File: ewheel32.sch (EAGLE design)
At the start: 201 parts, among them Q1 32.768kHz, Q2 8MHz, U1 MK22DX256VLF5, U10 MC74HC595ADTR2G, U11 MC74HC595ADTR2G, U12 MC74HC595ADTR2G, U13 MC74HC595ADTR2G, U14 MC74HC595ADTR2G, U15 MC74HC595ADTR2G, U16 MC74HC595ADTR2G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

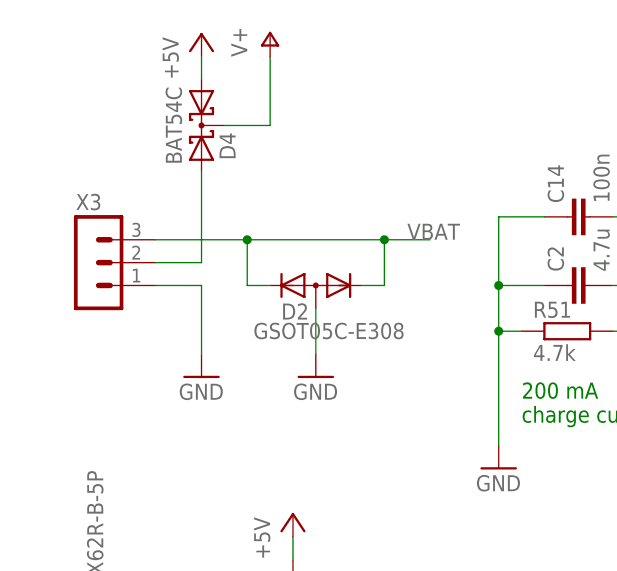
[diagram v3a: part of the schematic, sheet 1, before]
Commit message: VBAT and V+ are fixed.
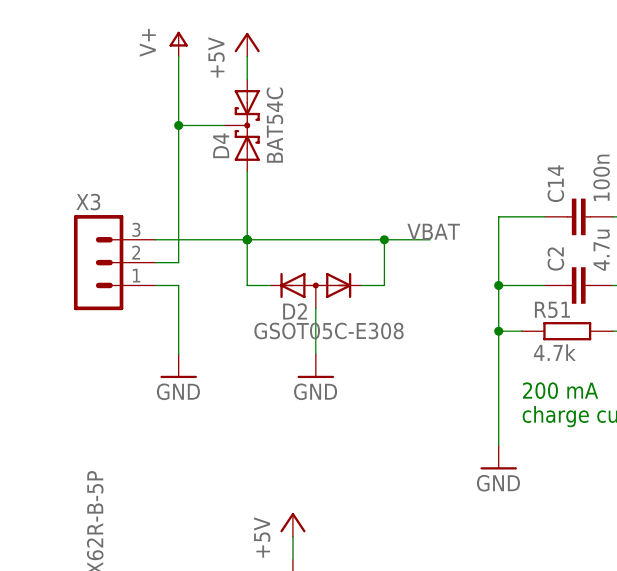
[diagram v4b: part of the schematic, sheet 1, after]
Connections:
- removed net N$6: D4.A2, X3.2
- net V+: now also X3.2
- net VBAT: now also D4.A2
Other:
- moved on the sheet: D4
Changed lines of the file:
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@@
 </instance>
 <instance part="X3" gate="G$1" x="17.78" y="226.06"/>
-<instance part="P+1" gate="1" x="38.1" y="251.46"/>
+<instance part="P+1" gate="1" x="27.94" y="251.46"/>
 <instance part="P+3" gate="1" x="203.2" y="233.68"/>
-<instance part="GND2" gate="1" x="30.48" y="213.36"/>
+<instance part="GND2" gate="1" x="27.94" y="213.36"/>
 <instance part="GND4" gate="1" x="93.98" y="203.2"/>
 <instance part="GND6" gate="1" x="144.78" y="35.56"/>
@@
 <instance part="GND49" gate="1" x="48.26" y="88.9"/>
 <instance part="D3" gate="G$1" x="43.18" y="111.76" rot="R270"/>
-<instance part="D4" gate="G$1" x="30.48" y="241.3" rot="R270"/>
+<instance part="D4" gate="G$1" x="35.56" y="241.3" rot="MR270"/>
 <instance part="C24" gate="G$1" x="55.88" y="142.24"/>
 <instance part="GND50" gate="1" x="55.88" y="132.08"/>
@@
 <instance part="R60" gate="G$1" x="116.84" y="241.3"/>
 <instance part="GND55" gate="1" x="124.46" y="236.22"/>
-<instance part="P+6" gate="1" x="30.48" y="251.46"/>
+<instance part="P+6" gate="1" x="35.56" y="251.46"/>
 </instances>
 <busses>
@@
 <segment>
 <pinref part="X3" gate="G$1" pin="1"/>
-<wire x1="25.4" y1="223.52" x2="30.48" y2="223.52" width="0.1524" layer="91"/>
-<wire x1="30.48" y1="223.52" x2="30.48" y2="215.9" width="0.1524" layer="91"/>
+<wire x1="25.4" y1="223.52" x2="27.94" y2="223.52" width="0.1524" layer="91"/>
+<wire x1="27.94" y1="223.52" x2="27.94" y2="215.9" width="0.1524" layer="91"/>
 <pinref part="GND2" gate="1" pin="GND"/>
 </segment>
@@
 <segment>
 <pinref part="P+1" gate="1" pin="V+"/>
-<wire x1="38.1" y1="248.92" x2="38.1" y2="241.3" width="0.1524" layer="91"/>
+<wire x1="27.94" y1="248.92" x2="27.94" y2="241.3" width="0.1524" layer="91"/>
 <pinref part="D4" gate="G$1" pin="CC"/>
-<wire x1="33.02" y1="241.3" x2="38.1" y2="241.3" width="0.1524" layer="91"/>
+<wire x1="33.02" y1="241.3" x2="27.94" y2="241.3" width="0.1524" layer="91"/>
+<pinref part="X3" gate="G$1" pin="2"/>
+<wire x1="25.4" y1="226.06" x2="27.94" y2="226.06" width="0.1524" layer="91"/>
+<wire x1="27.94" y1="226.06" x2="27.94" y2="241.3" width="0.1524" layer="91"/>
+<junction x="27.94" y="241.3"/>
 </segment>
 <segment>
@@
 <pinref part="D4" gate="G$1" pin="A1"/>
 <pinref part="P+6" gate="1" pin="+5V"/>
-<wire x1="30.48" y1="246.38" x2="30.48" y2="248.92" width="0.1524" layer="91"/>
+<wire x1="35.56" y1="246.38" x2="35.56" y2="248.92" width="0.1524" layer="91"/>
 </segment>
 </net>
@@
 <wire x1="38.1" y1="223.52" x2="35.56" y2="223.52" width="0.1524" layer="91"/>
 <wire x1="35.56" y1="223.52" x2="35.56" y2="228.6" width="0.1524" layer="91"/>
+<pinref part="D2" gate="G$1" pin="K1"/>
 <wire x1="35.56" y1="228.6" x2="25.4" y2="228.6" width="0.1524" layer="91"/>
-<pinref part="D2" gate="G$1" pin="K1"/>
 <wire x1="48.26" y1="223.52" x2="50.8" y2="223.52" width="0.1524" layer="91"/>
 <wire x1="50.8" y1="223.52" x2="50.8" y2="228.6" width="0.1524" layer="91"/>
@@
 <junction x="50.8" y="228.6"/>
 <label x="53.34" y="228.6" size="1.778" layer="95"/>
+<pinref part="D4" gate="G$1" pin="A2"/>
+<wire x1="35.56" y1="236.22" x2="35.56" y2="228.6" width="0.1524" layer="91"/>
+<junction x="35.56" y="228.6"/>
 </segment>
 <segment>
@@
 </segment>
 </net>
-<net name="N$6" class="0">
-<segment>
-<pinref part="D4" gate="G$1" pin="A2"/>
-<wire x1="30.48" y1="236.22" x2="30.48" y2="226.06" width="0.1524" layer="91"/>
-<pinref part="X3" gate="G$1" pin="2"/>
-<wire x1="30.48" y1="226.06" x2="25.4" y2="226.06" width="0.1524" layer="91"/>
-</segment>
-</net>

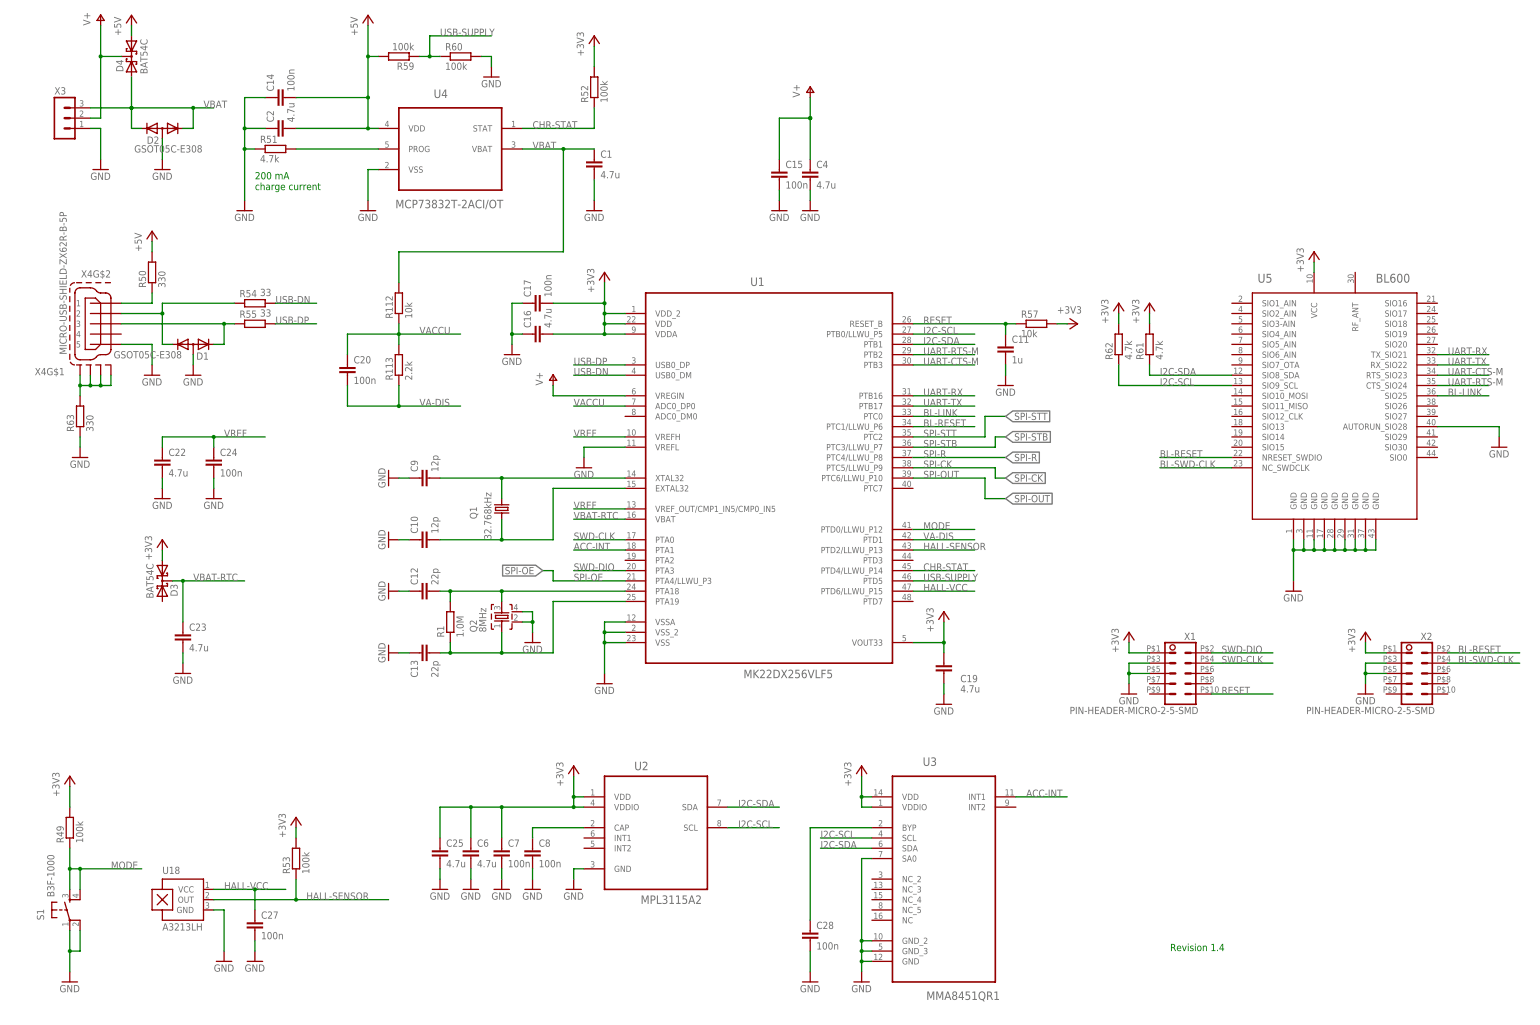
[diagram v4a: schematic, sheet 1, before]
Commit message: State RGB LED. Second Hall Sensor (ultra low power to wake up from deep sleep). Breakable PCB (MCU part / LED part). Pin head for I2C and SPI.
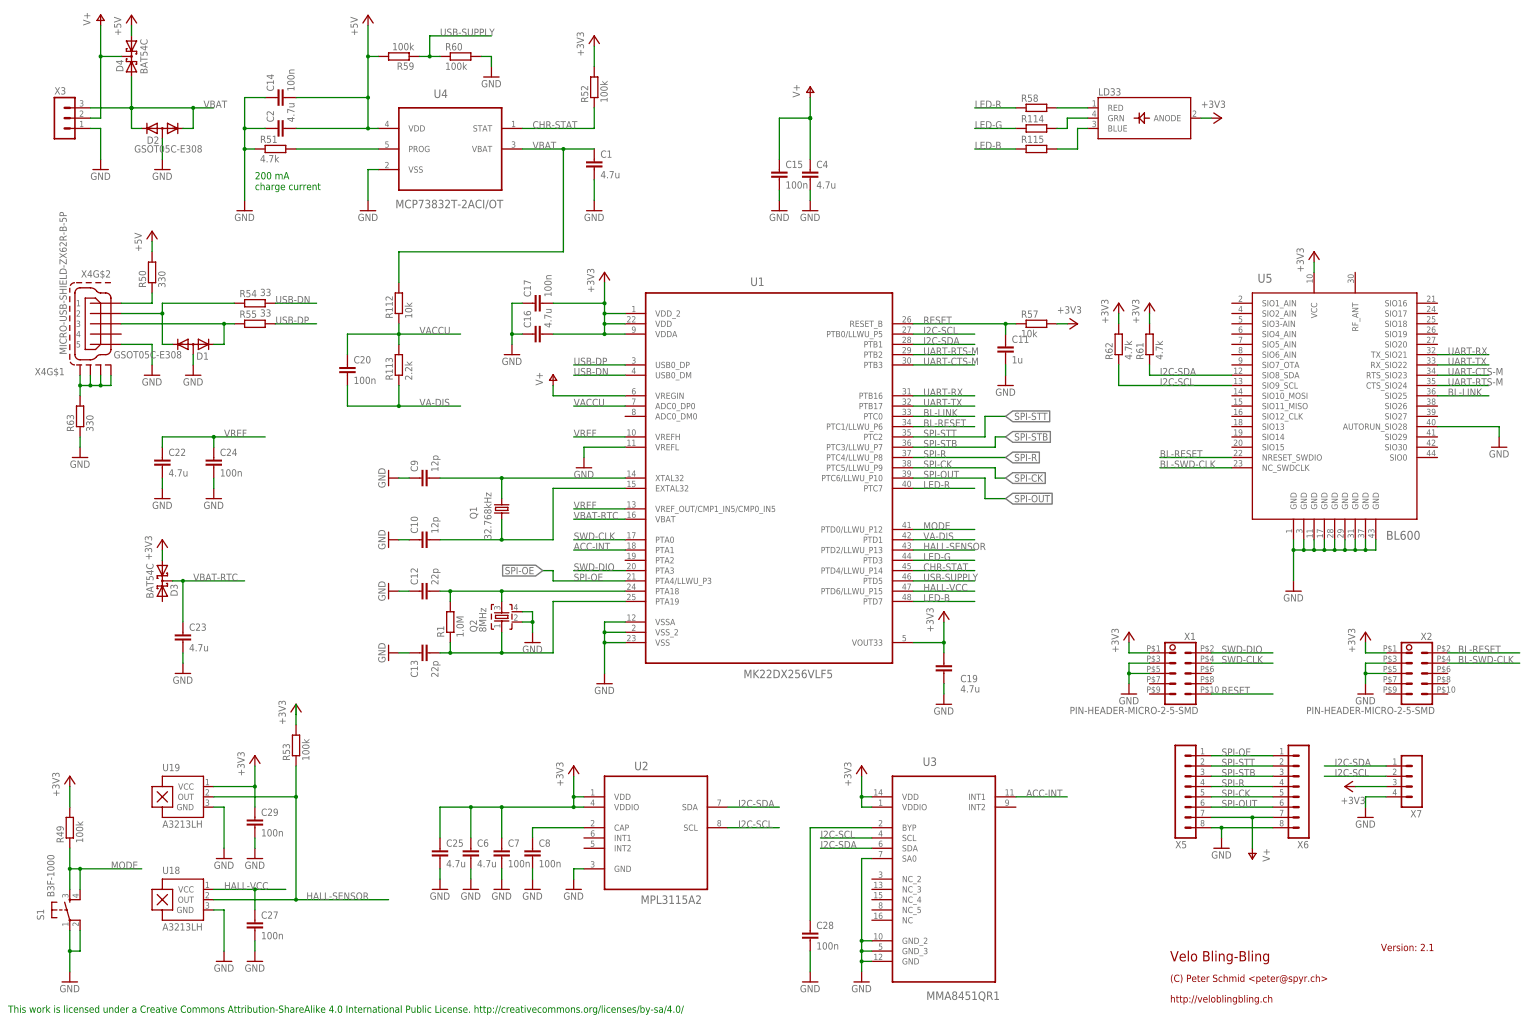
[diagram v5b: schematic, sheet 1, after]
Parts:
- added C29: 100n, resistor:C-EUC0805
- added LD33: CLV1A-FKB, freescale-uc:LED-RGB
- added R114, R115, R58: 220, resistor:R-EU_R0805
- added U19: A3213LH, allegro:A1381LH
- added X5, X6: (no value), con-lstb:MA08-1
- added X7: (no value), con-lstb:MA04-1
- C1, C11, C16, C18, C19, C2, C21, C22, C23, C25, C4, C6: device resistor:C-EUC1206 -> resistor:C-EUC0805
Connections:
- new net LED-B: R115.1, U1.PTD7
- new net LED-G: R114.1, U1.PTD3
- new net LED-R: R58.1, U1.PTC7
- new net N$6: LD33.GRN, R114.2
- new net N$7: LD33.RED, R58.2
- new net N$8: LD33.BLUE, R115.2
- net +3V3: now also C29.1, LD33.ANODE, U19.VCC, X7.3
- net GND: now also C29.2, U19.GND, X5.8, X6.8, X7.4
- net HALL-SENSOR: now also U19.OUT
- net I2C-SCL: now also X7.2
- net I2C-SDA: now also X7.1
- net SPI-CK: now also X5.5, X6.5
- net SPI-OE: now also X5.1, X6.1
- net SPI-OUT: now also X5.6, X6.6
- net SPI-R: now also X5.4, X6.4
- net SPI-STB: now also X5.3, X6.3
- net SPI-STT: now also X5.2, X6.2
- net V+: now also X5.7, X6.7
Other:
- note removed: "Revision 1.4"
- moved on the sheet: R53

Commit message: New Bluetooth Low Energy module BL652
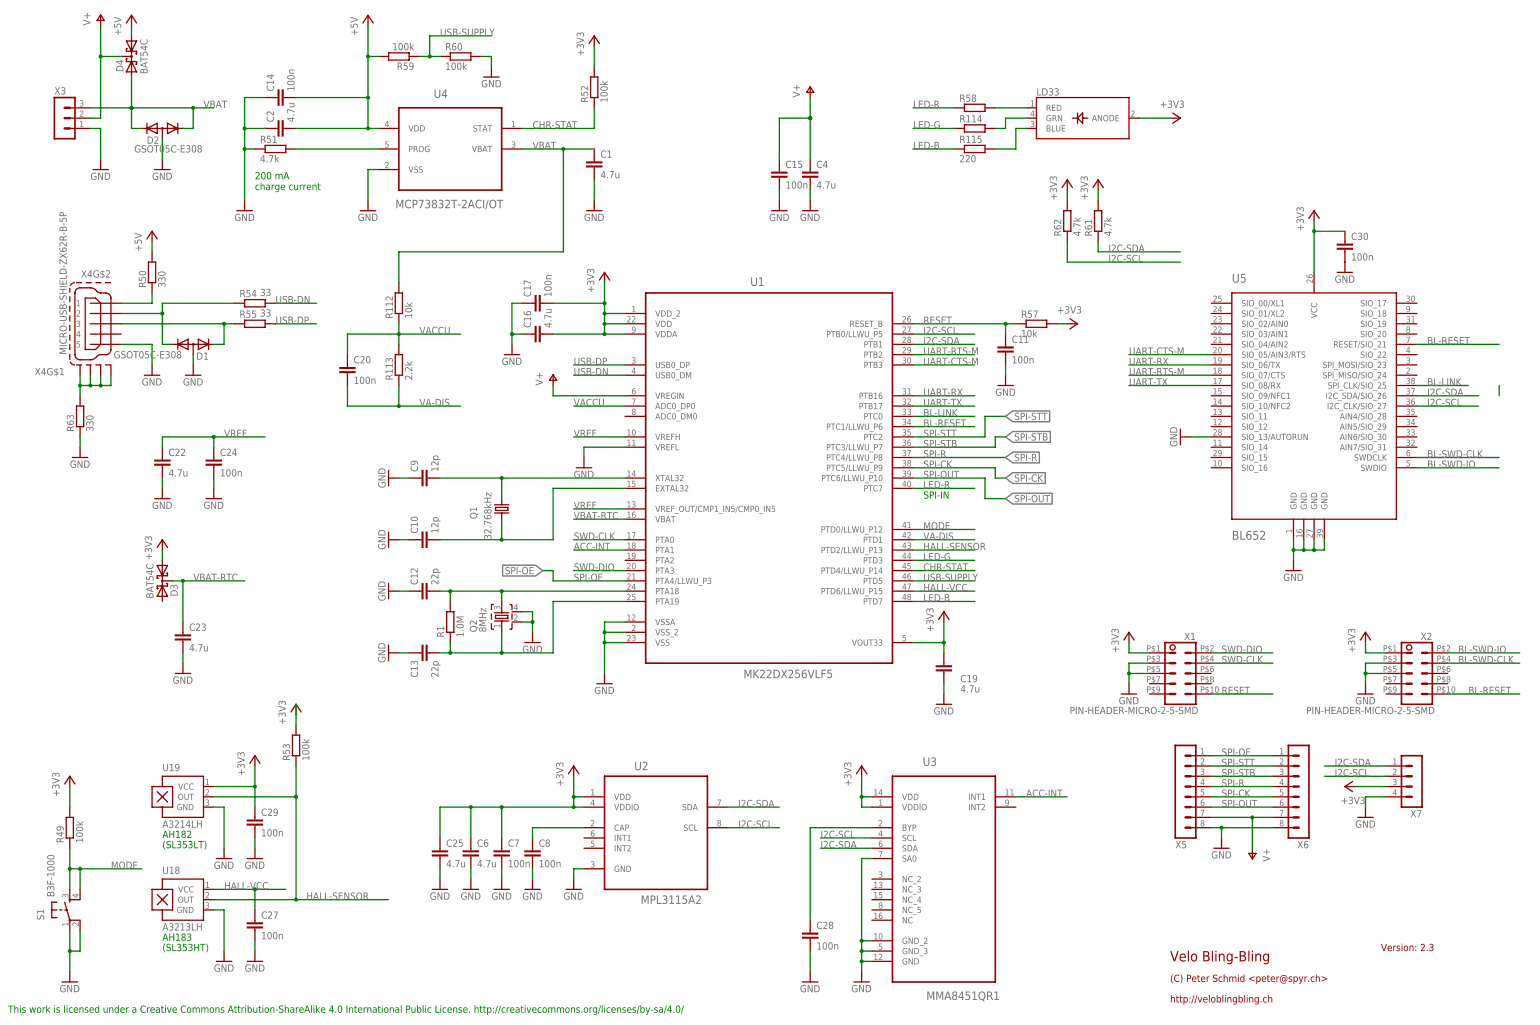
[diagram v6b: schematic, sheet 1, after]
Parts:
- added C30: 100n, resistor:C-EUC0805
- C11: value 1u -> 100n
- U19: value A3213LH -> A3214LH
- U5: value BL600 -> BL652; device ewheel32:LAIRD_BL600BL600XX -> ewheel32:LAIRD_BL652
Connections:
- new net BL-SWD-IO: U5.SWDIO, X2.2
- net +3V3: now also C30.1
- net BL-LINK: now also U5.SPI_CLK/SIO_25; no longer U5.SIO25
- net BL-RESET: now also U5.RESET/SIO_21, X2.10; no longer U5.NRESET_SWDIO, X2.2
- net BL-SWD-CLK: now also U5.SWDCLK; no longer U5.NC_SWDCLK
- net GND: now also C30.2, U5.SIO_13/AUTORUN; no longer U5.AUTORUN_SIO28, U5.GND@4, U5.GND@5, U5.GND@6, U5.GND@7, U5.GND@8
- net I2C-SCL: now also U5.I2C_CLK/SIO_27; no longer U5.SIO9_SCL
- net I2C-SDA: now also U5.I2C_SDA/SIO_26; no longer U5.SIO8_SDA
- net UART-CTS-M: now also U5.SIO_05/AIN3/RTS; no longer U5.RTS_SIO23
- net UART-RTS-M: now also U5.SIO_07/CTS; no longer U5.CTS_SIO24
- net UART-RX: now also U5.SIO_06/TX; no longer U5.TX_SIO21
- net UART-TX: now also U5.SIO_08/RX; no longer U5.RX_SIO22
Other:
- note added: "(SL353HT)"
- note added: "(SL353LT)"
- note added: "AH182"
- note added: "AH183"
- note added: "SPI-IN"
- moved on the sheet: LD33, R114, R115, R58, R61, R62
